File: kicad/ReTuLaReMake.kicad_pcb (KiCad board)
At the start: 2 copper layers, 54 x 26 mm, 26 parts, among them J1 40 Pin DIP Header, J2 Conn_02x05_Odd_Even, J3 Conn_01x01_Male, U1 ATF1508AS-10AU100

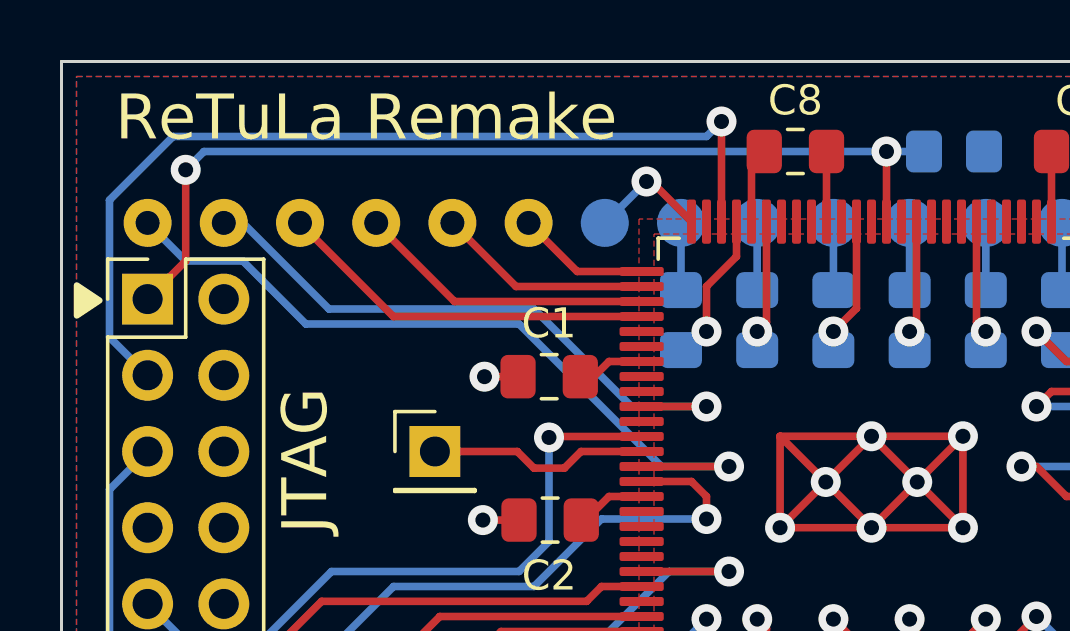
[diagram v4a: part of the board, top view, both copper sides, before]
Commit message: KiCAD: Remove GNDs on unused I/Os
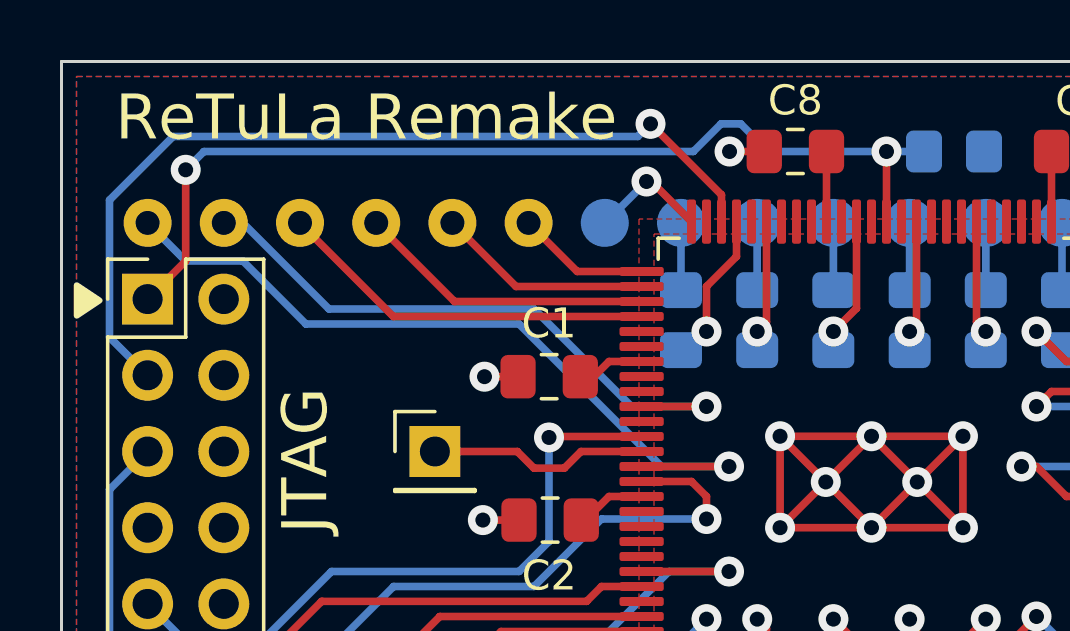
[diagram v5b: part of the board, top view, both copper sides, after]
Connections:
- U1 pad 10: GND -> unconnected-(U1-Pad10)
- U1 pad 13: GND -> unconnected-(U1-Pad13)
- U1 pad 14: GND -> unconnected-(U1-Pad14)
- U1 pad 17: GND -> unconnected-(U1-Pad17)
- U1 pad 20: GND -> unconnected-(U1-Pad20)
- U1 pad 21: GND -> unconnected-(U1-Pad21)
- U1 pad 23: GND -> unconnected-(U1-Pad23)
- U1 pad 24: GND -> unconnected-(U1-Pad24)
- U1 pad 28: GND -> unconnected-(U1-Pad28)
- U1 pad 30: GND -> unconnected-(U1-Pad30)
- U1 pad 31: GND -> unconnected-(U1-Pad31)
- U1 pad 32: GND -> unconnected-(U1-Pad32)
- U1 pad 33: GND -> unconnected-(U1-Pad33)
- U1 pad 36: GND -> unconnected-(U1-Pad36)
- U1 pad 37: GND -> unconnected-(U1-Pad37)
- U1 pad 40: GND -> unconnected-(U1-Pad40)
- U1 pad 41: GND -> unconnected-(U1-Pad41)
- U1 pad 45: GND -> unconnected-(U1-Pad45)
- U1 pad 5: GND -> unconnected-(U1-Pad5)
- U1 pad 50: GND -> unconnected-(U1-Pad50)
- U1 pad 52: GND -> unconnected-(U1-Pad52)
- U1 pad 53: GND -> unconnected-(U1-Pad53)
- U1 pad 54: GND -> unconnected-(U1-Pad54)
- U1 pad 55: GND -> unconnected-(U1-Pad55)
- U1 pad 57: GND -> unconnected-(U1-Pad57)
- U1 pad 58: GND -> unconnected-(U1-Pad58)
- U1 pad 61: GND -> unconnected-(U1-Pad61)
- U1 pad 63: GND -> unconnected-(U1-Pad63)
- U1 pad 65: GND -> unconnected-(U1-Pad65)
- U1 pad 67: GND -> unconnected-(U1-Pad67)
- U1 pad 68: GND -> unconnected-(U1-Pad68)
- U1 pad 69: GND -> unconnected-(U1-Pad69)
- U1 pad 7: GND -> unconnected-(U1-Pad7)
- U1 pad 71: GND -> unconnected-(U1-Pad71)
- U1 pad 8: GND -> unconnected-(U1-Pad8)
- U1 pad 80: GND -> unconnected-(U1-Pad80)
- U1 pad 81: GND -> unconnected-(U1-Pad81)
- U1 pad 83: GND -> unconnected-(U1-Pad83)
- U1 pad 84: GND -> unconnected-(U1-Pad84)
- U1 pad 9: GND -> unconnected-(U1-Pad9)
- U1 pad 92: GND -> unconnected-(U1-Pad92)
- U1 pad 93: GND -> unconnected-(U1-Pad93)
- U1 pad 94: GND -> unconnected-(U1-Pad94)
- U1 pad 98: GND -> unconnected-(U1-Pad98)
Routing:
- net /TDO: track 31.2 -> 29.7 mm
- net /TCK: track 32.0 -> 32.8 mm
- net GND: track 48.7 -> 47.9 mm, vias 15 -> 17

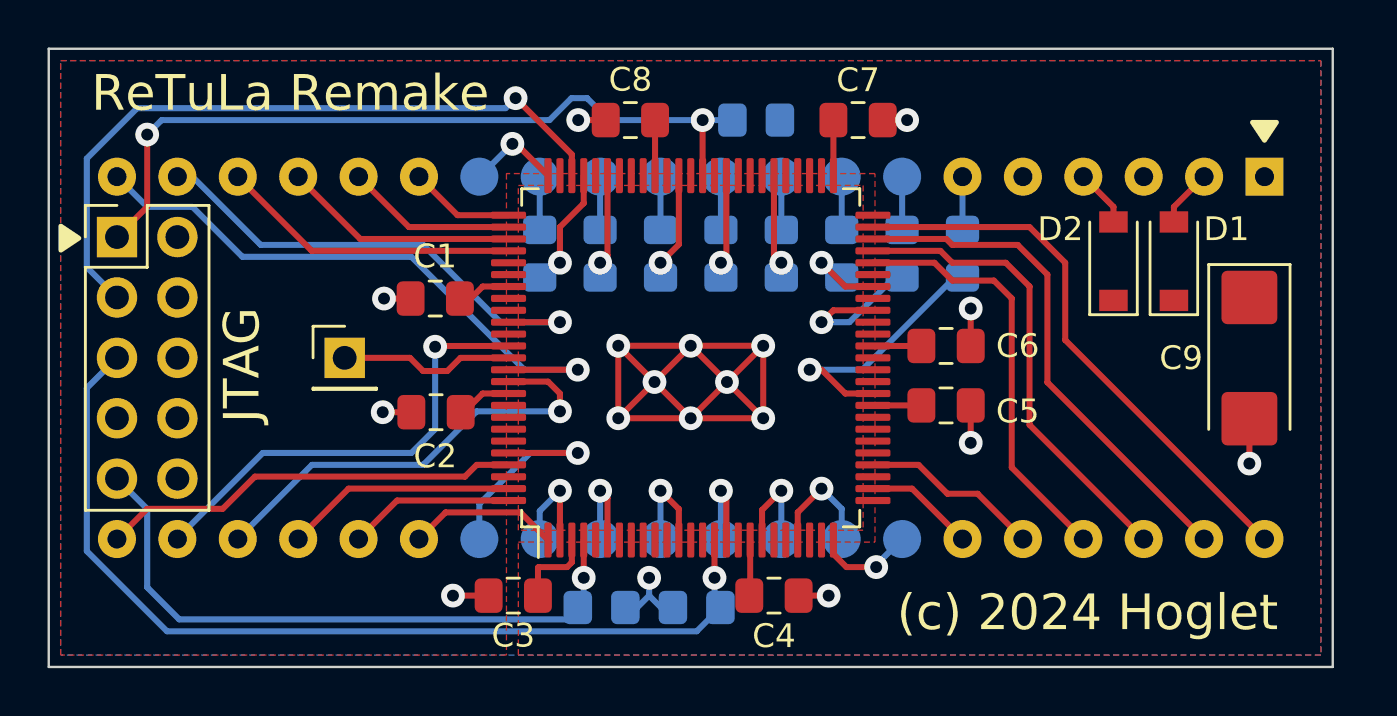
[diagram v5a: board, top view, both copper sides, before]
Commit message: KiCAD: Add clock filter; adjust decoupling
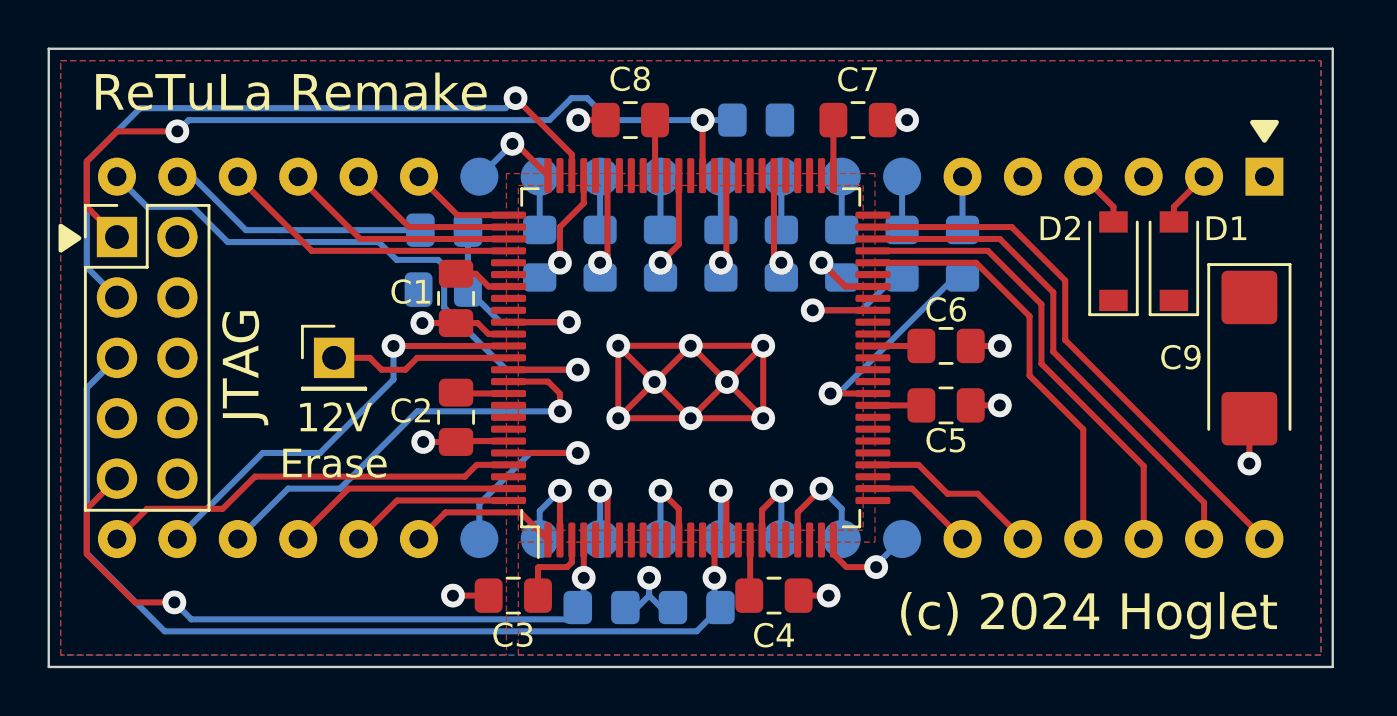
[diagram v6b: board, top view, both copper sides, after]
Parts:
- added C10: 47p, Capacitor_SMD:C_0805_2012Metric_Pad1.18x1.45mm_HandSolder, B.Cu at (116.6, 116.5)
- added R9: 120R, Resistor_SMD:R_0805_2012Metric_Pad1.20x1.40mm_HandSolder, B.Cu at (116.6, 114.0)
- moved C1 0.87 mm to (117.1, 116.9), turned to -90 degrees
- moved C2 0.87 mm to (117.1, 121.9), turned to -90 degrees
- moved J3 0.45 mm to (112.0, 119.4)
- renumbered R9 to R12
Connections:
- U1 pad 85: /HO2 -> /HO2filtered
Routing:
- net /HO2filtered: track 0.00 -> 9.86 mm, vias 0 -> 1
- net /HO2: track 20.2 -> 10.5 mm, vias 1 -> 0
- net GND: track 47.9 -> 52.2 mm
- net /TCK: track 32.8 -> 34.7 mm
- net /HD0: track 10.8 -> 9.02 mm
- net /TDI: track 26.9 -> 28.3 mm, vias 1 -> 2
- net /PNRDS: track 19.3 -> 18.1 mm
- net /HRST: track 25.7 -> 26.7 mm
- net /PD1: track 4.25 -> 3.66 mm
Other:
- board text added: "12V Erase"

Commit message: KiCAD: Update header to have four more thru-hole pins
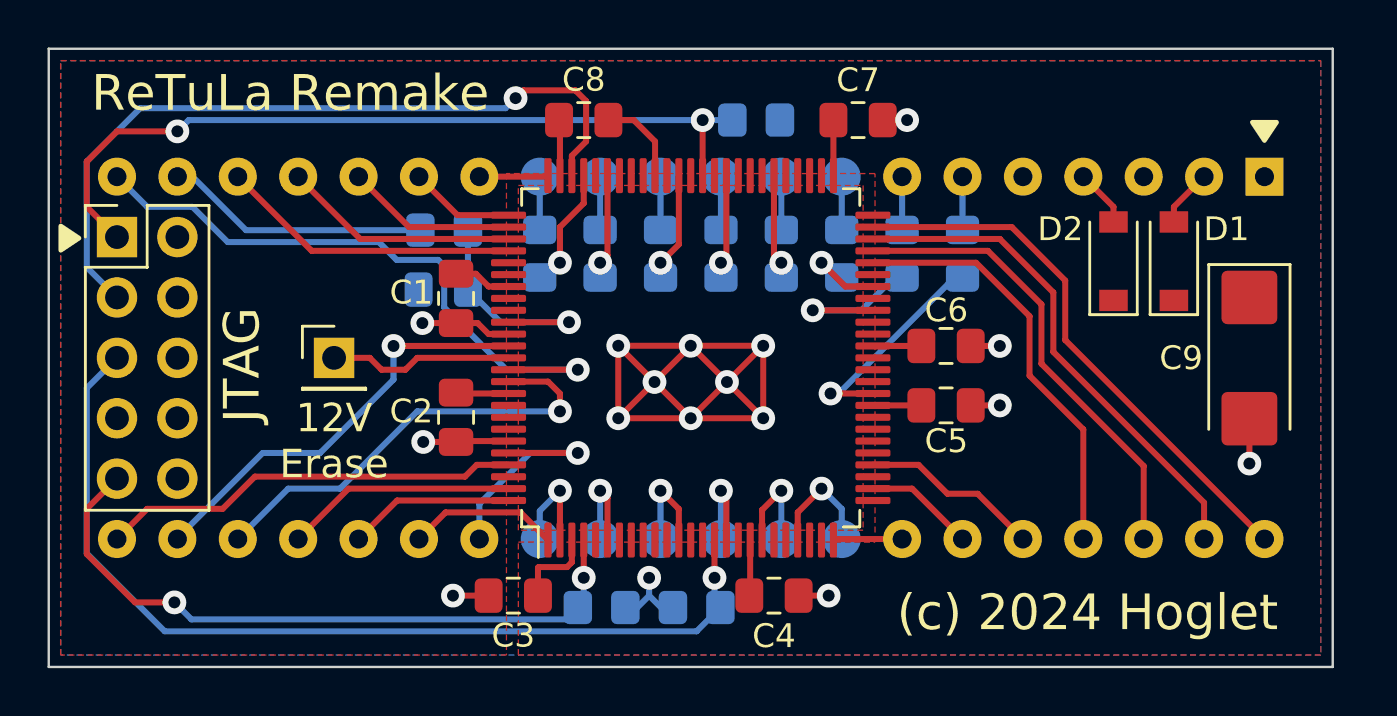
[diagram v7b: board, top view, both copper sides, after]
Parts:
- moved C8 1.96 mm to (122.5, 109.4)
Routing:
- net /TDO: track 29.6 -> 32.1 mm
- net VCC: track 22.4 -> 23.9 mm
- net GND: track 52.2 -> 53.4 mm, vias 17 -> 16
- net /HA0: track 4.01 -> 2.91 mm, vias 1 -> 0
- net /TCK: track 34.7 -> 33.9 mm
- net /PD1: track 3.66 -> 2.91 mm, vias 1 -> 0

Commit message: KiCAD: Improve C7/8 routing
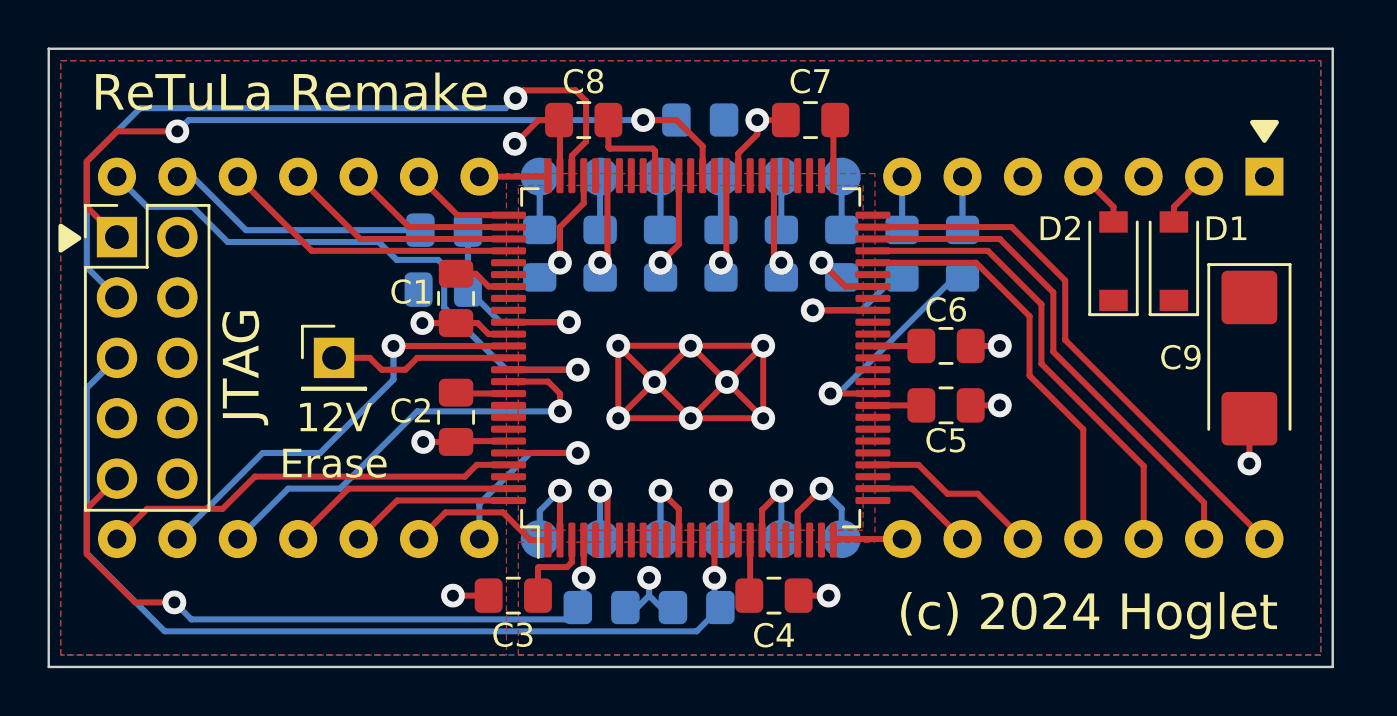
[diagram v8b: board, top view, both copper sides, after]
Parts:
- moved R12 2.35 mm to (127.4, 109.4)
- moved C7 2.00 mm to (132.0, 109.4), turned to 180 degrees
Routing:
- net GND: track 53.4 -> 58.5 mm, vias 16 -> 17
